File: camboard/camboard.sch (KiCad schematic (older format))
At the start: 7 parts

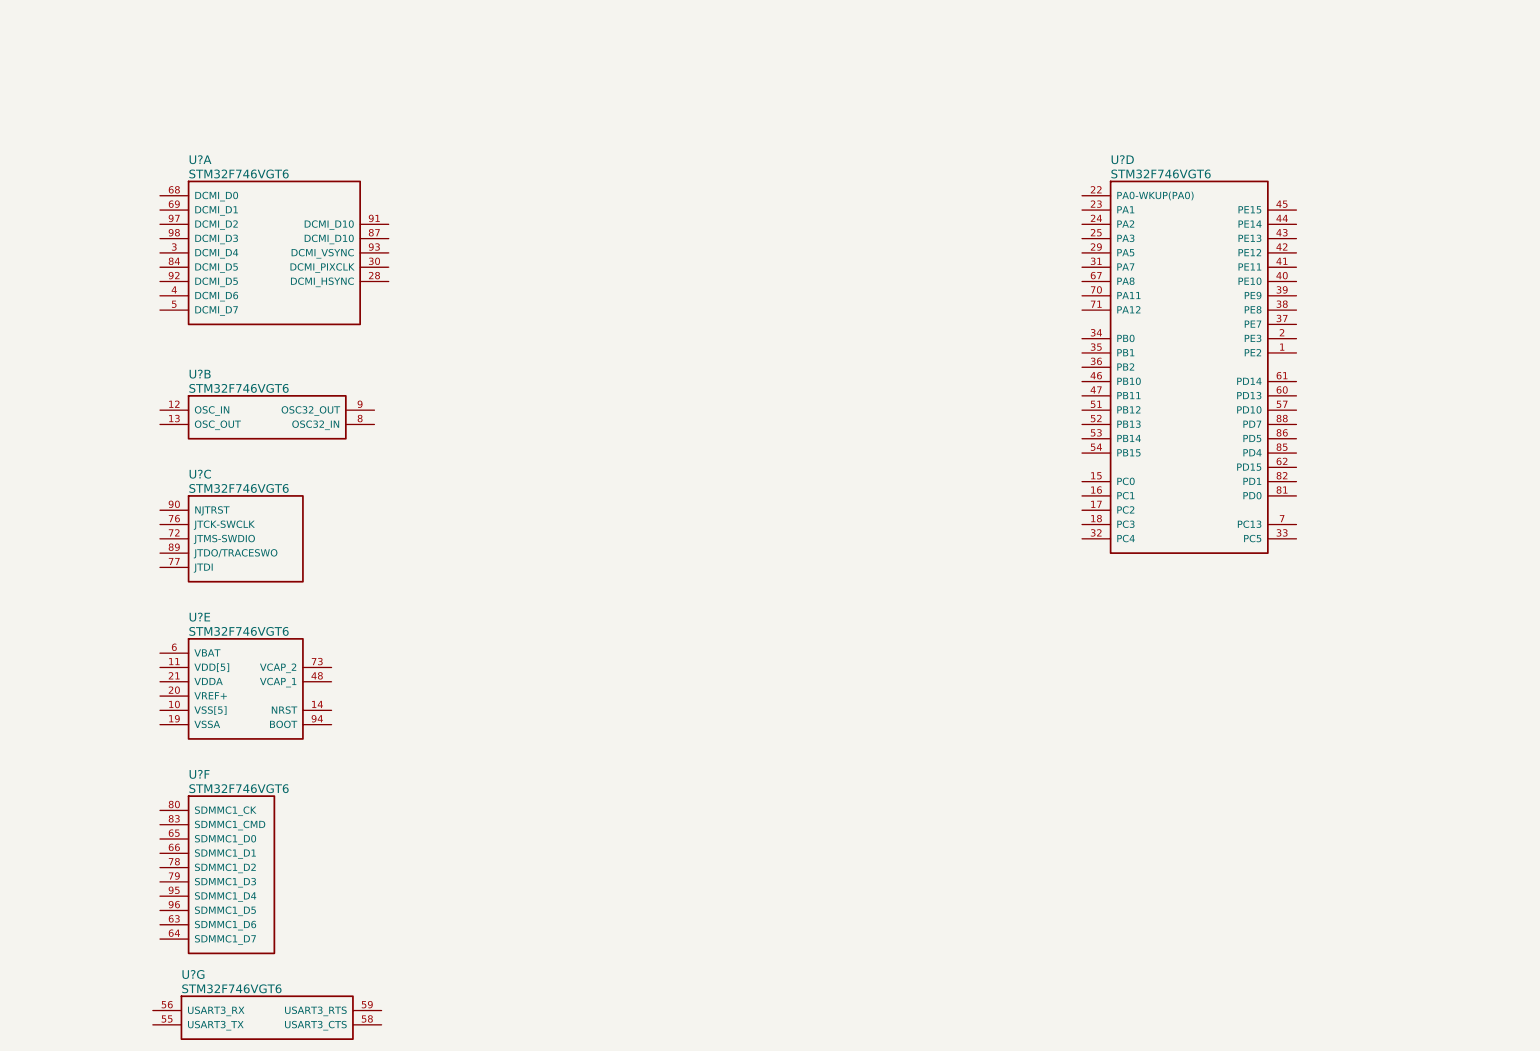
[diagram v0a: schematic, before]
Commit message: added oscillators
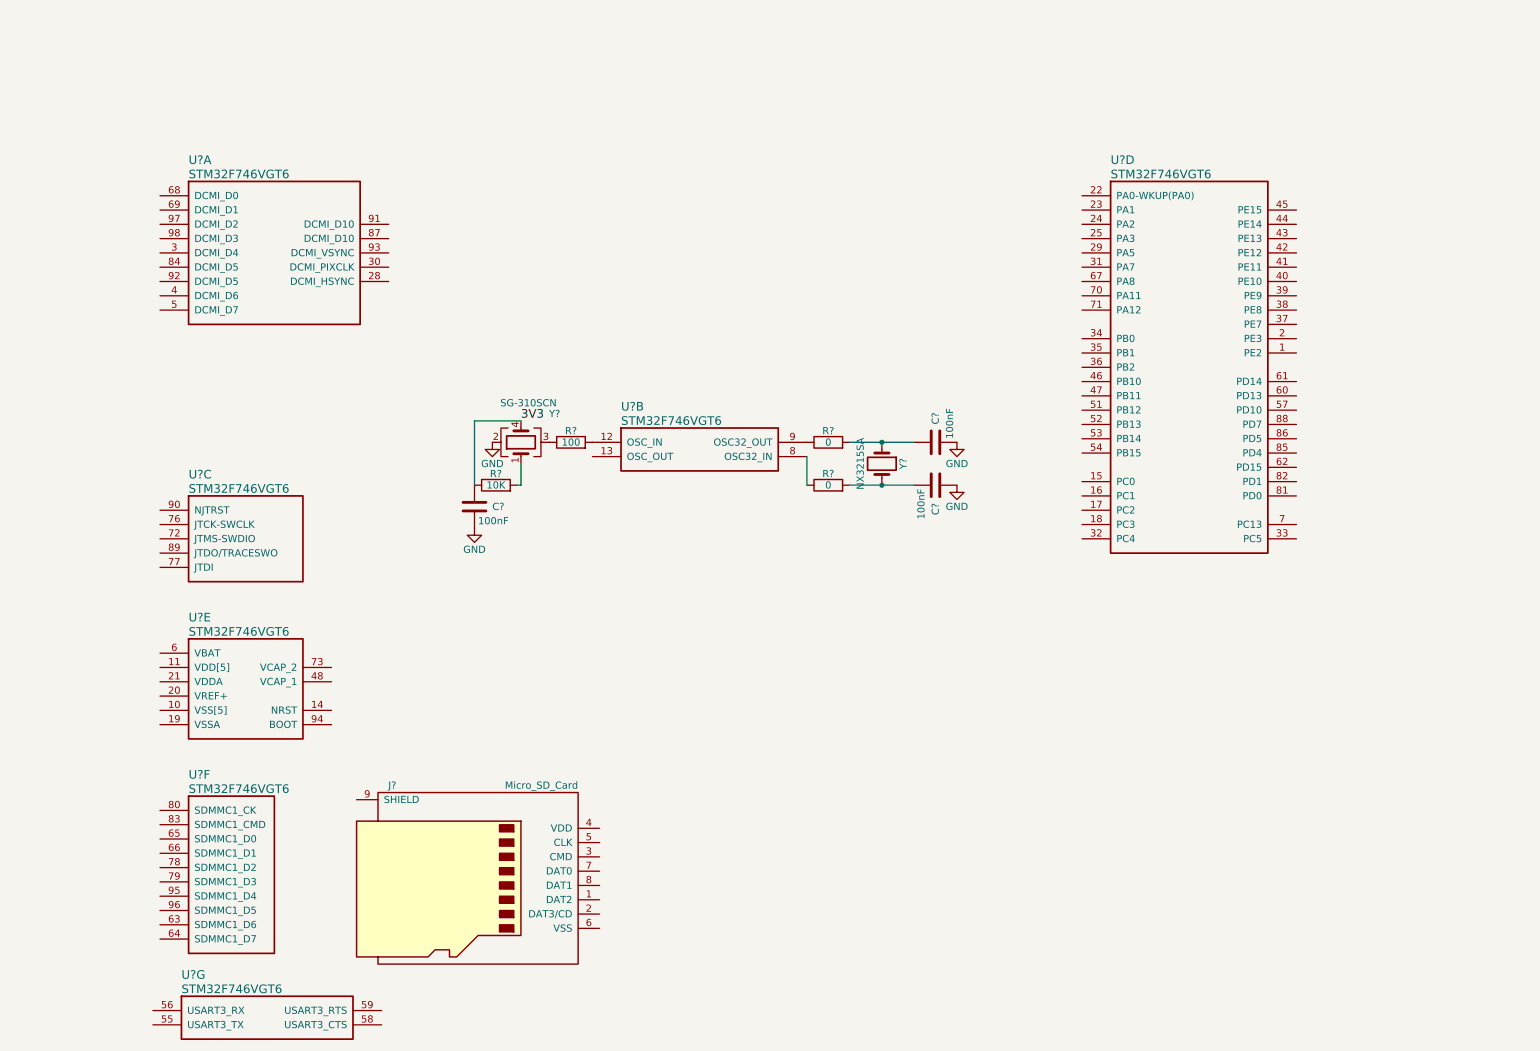
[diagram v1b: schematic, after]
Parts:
- added C? (x3): 100nF, symbol C
- added J?: Micro_SD_Card, symbol Micro_SD_Card
- added R?: 10K, symbol R
- added R?: 100, symbol R
- added R? (x2): 0, symbol R
- added Y?: SG-310SCN, symbol Crystal_GND23
- added Y?: NX3215SA, symbol Crystal
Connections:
- net at U?.12 (OSC_IN): now also R?.2
- net at U?.8 (OSC32_IN): now also R?.1
- net at U?.9 (OSC32_OUT): now also R?.1
- new net: R?.2, Y?.1
- new net: R?.1, Y?.3
- new net: C?.1, R?.2, Y?.1
- new net: C?.2, R?.2, Y?.2
- new net 3V3: C?.1, R?.1, Y?.4
- new net GND: C?.1, C?.2, C?.2, Y?.2
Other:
- moved on the sheet: U?B
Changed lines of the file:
@@
 LIBS:STM32F7x
 LIBS:stm32-v2
+LIBS:114-00841-68-1-nd
 LIBS:camboard-cache
 EELAYER 25 0
@@
 L STM32F746VGT6 U?
 U 2 1 59CAFB26
-P 1300 3250
-F 0 "U?" H 1500 3500 60  0000 L CNN
-F 1 "STM32F746VGT6" H 1500 3400 60  0000 L CNN
-F 2 "" H 1300 3250 60  0001 C CNN
-F 3 "" H 1300 3250 60  0001 C CNN
-	2    1300 3250
+P 4325 3475
+F 0 "U?" H 4525 3725 60  0000 L CNN
+F 1 "STM32F746VGT6" H 4525 3625 60  0000 L CNN
+F 2 "" H 4325 3475 60  0001 C CNN
+F 3 "" H 4325 3475 60  0001 C CNN
+	2    4325 3475
 	1    0    0    -1
 $EndComp
@@
 	1    0    0    -1
 $EndComp
+$Comp
+L Micro_SD_Card J?
+U 1 1 59CBBC6A
+P 3575 6475
+F 0 "J?" H 2925 7075 50  0000 C CNN
+F 1 "Micro_SD_Card" H 4225 7075 50  0000 R CNN
+F 2 "" H 4725 6775 50  0001 C CNN
+F 3 "" H 3575 6475 50  0001 C CNN
+	1    3575 6475
+	1    0    0    -1
+$EndComp
+$Comp
+L Crystal_GND23 Y?
+U 1 1 59CBC17B
+P 3825 3475
+F 0 "Y?" V 4025 3200 50  0000 L CNN
+F 1 "SG-310SCN" V 4100 3225 50  0000 L CNN
+F 2 "" H 3825 3475 50  0001 C CNN
+F 3 "" H 3825 3475 50  0001 C CNN
+	1    3825 3475
+	0    -1   -1   0
+$EndComp
+$Comp
+L Crystal Y?
+U 1 1 59CBC1BE
+P 6350 3625
+F 0 "Y?" H 6350 3775 50  0000 C CNN
+F 1 "NX3215SA" H 6350 3475 50  0000 C CNN
+F 2 "" H 6350 3625 50  0001 C CNN
+F 3 "" H 6350 3625 50  0001 C CNN
+	1    6350 3625
+	0    1    1    0
+$EndComp
+$Comp
+L GND #PWR?
+U 1 1 59CBC3C5
+P 3500 4075
+F 0 "#PWR?" H 3500 3825 50  0001 C CNN
+F 1 "GND" H 3500 3925 50  0000 C CNN
+F 2 "" H 3500 4075 50  0001 C CNN
+F 3 "" H 3500 4075 50  0001 C CNN
+	1    3500 4075
+	1    0    0    -1
+$EndComp
+$Comp
+L R R?
+U 1 1 59CBC4FC
+P 3650 3775
+F 0 "R?" V 3730 3775 50  0000 C CNN
+F 1 "10K" V 3650 3775 50  0000 C CNN
+F 2 "" V 3580 3775 50  0001 C CNN
+F 3 "" H 3650 3775 50  0001 C CNN
+	1    3650 3775
+	0    -1   -1   0
+$EndComp
+$Comp
+L C C?
+U 1 1 59CBC717
+P 3500 3925
+F 0 "C?" H 3625 3925 50  0000 L CNN
+F 1 "100nF" H 3525 3825 50  0000 L CNN
+F 2 "" H 3538 3775 50  0001 C CNN
+F 3 "" H 3500 3925 50  0001 C CNN
+	1    3500 3925
+	1    0    0    -1
+$EndComp
+Text Label 3825 3325 0    60   ~ 0
+3V3
+$Comp
+L GND #PWR?
+U 1 1 59CBC971
+P 3625 3475
+F 0 "#PWR?" H 3625 3225 50  0001 C CNN
+F 1 "GND" H 3625 3325 50  0000 C CNN
+F 2 "" H 3625 3475 50  0001 C CNN
+F 3 "" H 3625 3475 50  0001 C CNN
+	1    3625 3475
+	1    0    0    -1
+$EndComp
+$Comp
+L R R?
+U 1 1 59CBCF2D
+P 4175 3475
+F 0 "R?" V 4255 3475 50  0000 C CNN
+F 1 "100" V 4175 3475 50  0000 C CNN
+F 2 "" V 4105 3475 50  0001 C CNN
+F 3 "" H 4175 3475 50  0001 C CNN
+	1    4175 3475
+	0    -1   -1   0
+$EndComp
+$Comp
+L R R?
+U 1 1 59CBD411
+P 5975 3475
+F 0 "R?" V 6055 3475 50  0000 C CNN
+F 1 "0" V 5975 3475 50  0000 C CNN
+F 2 "" V 5905 3475 50  0001 C CNN
+F 3 "" H 5975 3475 50  0001 C CNN
+	1    5975 3475
+	0    -1   -1   0
+$EndComp
+$Comp
+L R R?
+U 1 1 59CBD485
+P 5975 3775
+F 0 "R?" V 6055 3775 50  0000 C CNN
+F 1 "0" V 5975 3775 50  0000 C CNN
+F 2 "" V 5905 3775 50  0001 C CNN
+F 3 "" H 5975 3775 50  0001 C CNN
+	1    5975 3775
+	0    -1   -1   0
+$EndComp
+Wire Wire Line
+	3825 3325 3500 3325
+Wire Wire Line
+	3500 3325 3500 3775
+Wire Wire Line
+	3800 3775 3825 3775
+Wire Wire Line
+	3825 3775 3825 3625
+Wire Wire Line
+	6125 3475 6575 3475
+Wire Wire Line
+	6125 3775 6575 3775
+$Comp
+L C C?
+U 1 1 59CBD71A
+P 6725 3475
+F 0 "C?" H 6850 3475 50  0000 L CNN
+F 1 "100nF" H 6750 3375 50  0000 L CNN
+F 2 "" H 6763 3325 50  0001 C CNN
+F 3 "" H 6725 3475 50  0001 C CNN
+	1    6725 3475
+	0    -1   -1   0
+$EndComp
+$Comp
+L C C?
+U 1 1 59CBD7BA
+P 6725 3775
+F 0 "C?" H 6850 3775 50  0000 L CNN
+F 1 "100nF" H 6750 3675 50  0000 L CNN
+F 2 "" H 6763 3625 50  0001 C CNN
+F 3 "" H 6725 3775 50  0001 C CNN
+	1    6725 3775
+	0    1    1    0
+$EndComp
+Connection ~ 6350 3475
+Connection ~ 6350 3775
+$Comp
+L GND #PWR?
+U 1 1 59CBD8AB
+P 6875 3475
+F 0 "#PWR?" H 6875 3225 50  0001 C CNN
+F 1 "GND" H 6875 3325 50  0000 C CNN
+F 2 "" H 6875 3475 50  0001 C CNN
+F 3 "" H 6875 3475 50  0001 C CNN
+	1    6875 3475
+	1    0    0    -1
+$EndComp
+$Comp
+L GND #PWR?
+U 1 1 59CBD8FA
+P 6875 3775
+F 0 "#PWR?" H 6875 3525 50  0001 C CNN
+F 1 "GND" H 6875 3625 50  0000 C CNN
+F 2 "" H 6875 3775 50  0001 C CNN
+F 3 "" H 6875 3775 50  0001 C CNN
+	1    6875 3775
+	1    0    0    -1
+$EndComp
+Wire Wire Line
+	5825 3575 5825 3775
 $EndSCHEMATC

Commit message: fixed wrong library reference and added power select
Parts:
- removed J?: Micro_SD_Card, symbol Micro_SD_Card
- added BT?: Battery, symbol Battery
- added SW?: JS202011SCQN, symbol SW_DPDT_x2
- added U?: MCP1703A-3302_SOT23, TO_SOT_Packages_SMD:SOT-23, symbol MCP1703A-3302_SOT23
- added U?: FT230XS, SSOP-16, symbol FT230XS
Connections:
- net labels added: USB_3V3
- wire segments 7 -> 9
- no-connect marks 0 -> 5
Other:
- moved on the sheet: C?, R?, U?A, U?B, U?C, U?E, U?F, U?G, Y?

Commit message: more connections
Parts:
- removed BT?: Battery, symbol Battery
- removed SW?: JS202011SCQN, symbol SW_DPDT_x2
- added J?: Micro_SD_Card, symbol Micro_SD_Card
- added SW?: SW_DPDT_x2, Buttons_Switches_THT:SW_CuK_JS202011CQN_DPDT_Straight, symbol SW_DPDT_x2
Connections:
- net labels added: +3V3, USB_5V, VIN
- net labels removed: 3V3, USB_3V3
- wire segments 9 -> 19
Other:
- moved on the sheet: U?, U?F, U?G
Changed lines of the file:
@@
 L STM32F746VGT6 U?
 U 7 1 59CAFE6F
-P 625 6800
-F 0 "U?" H 825 7050 60  0000 L CNN
-F 1 "STM32F746VGT6" H 825 6950 60  0000 L CNN
-F 2 "" H 625 6800 60  0001 C CNN
-F 3 "" H 625 6800 60  0001 C CNN
-	7    625  6800
-	1    0    0    -1
+P 7125 4425
+F 0 "U?" H 7350 4150 60  0000 L CNN
+F 1 "STM32F746VGT6" H 7550 4150 60  0000 L CNN
+F 2 "" H 7125 4425 60  0001 C CNN
+F 3 "" H 7125 4425 60  0001 C CNN
+	7    7125 4425
+	-1   0    0    -1
 $EndComp
 $Comp
@@
 P 7700 5400
 F 0 "Y?" V 7900 5125 50  0000 L CNN
-F 1 "SG-310SCN" V 7975 5150 50  0000 L CNN
+F 1 "SG-310SCN" V 8150 5200 50  0000 L CNN
 F 2 "" H 7700 5400 50  0001 C CNN
 F 3 "" H 7700 5400 50  0001 C CNN
@@
 	1    0    0    -1
 $EndComp
-Text Label 7700 5250 0    60   ~ 0
-3V3
 $Comp
 L GND #PWR?
@@
 Wire Wire Line
 	9700 5500 9700 5700
-NoConn ~ 775  6300
-NoConn ~ 775  6200
+NoConn ~ 3900 6925
+NoConn ~ 3900 6825
 $Comp
 L STM32F746VGT6 U?
 U 6 1 59CAFD02
-P 775 5400
-F 0 "U?" H 975 5650 60  0000 L CNN
-F 1 "STM32F746VGT6" H 975 5550 60  0000 L CNN
-F 2 "" H 775 5400 60  0001 C CNN
-F 3 "" H 775 5400 60  0001 C CNN
-	6    775  5400
-	1    0    0    -1
-$EndComp
-NoConn ~ 775  6100
-NoConn ~ 775  6000
+P 3900 6025
+F 0 "U?" H 4100 6275 60  0000 L CNN
+F 1 "STM32F746VGT6" H 4100 6175 60  0000 L CNN
+F 2 "" H 3900 6025 60  0001 C CNN
+F 3 "" H 3900 6025 60  0001 C CNN
+	6    3900 6025
+	1    0    0    -1
+$EndComp
+NoConn ~ 3900 6725
+NoConn ~ 3900 6625
 $Comp
 L MCP1703A-3302_SOT23 U?
 U 1 1 59CBD041
-P 1150 850
-F 0 "U?" H 1000 975 50  0000 C CNN
-F 1 "MCP1703A-3302_SOT23" H 575 1075 50  0000 L CNN
-F 2 "TO_SOT_Packages_SMD:SOT-23" H 1150 1050 50  0001 C CNN
-F 3 "" H 1150 800 50  0001 C CNN
-	1    1150 850
+P 2725 875
+F 0 "U?" H 2575 1000 50  0000 C CNN
+F 1 "MCP1703A-3302_SOT23" H 2300 1175 50  0000 L CNN
+F 2 "TO_SOT_Packages_SMD:SOT-23" H 2725 1075 50  0001 C CNN
+F 3 "" H 2725 825 50  0001 C CNN
+	1    2725 875
 	1    0    0    -1
 $EndComp
@@
 	1    0    0    -1
 $EndComp
-$Comp
-L Battery BT?
-U 1 1 59CBD1E1
-P 850 1050
-F 0 "BT?" H 600 1150 50  0000 L CNN
-F 1 "Battery" H 500 1050 50  0000 L CNN
-F 2 "" V 850 1110 50  0001 C CNN
-F 3 "" V 850 1110 50  0001 C CNN
-	1    850  1050
-	1    0    0    -1
-$EndComp
-Wire Wire Line
-	850  1250 1150 1250
-Wire Wire Line
-	1150 1250 1150 1150
+Text Label 2025 975  2    60   ~ 0
+USB_5V
+$Comp
+L GND #PWR?
+U 1 1 59CBCD24
+P 4725 5325
+F 0 "#PWR?" H 4725 5075 50  0001 C CNN
+F 1 "GND" H 4725 5175 50  0000 C CNN
+F 2 "" H 4725 5325 50  0001 C CNN
+F 3 "" H 4725 5325 50  0001 C CNN
+	1    4725 5325
+	1    0    0    -1
+$EndComp
+$Comp
+L GND #PWR?
+U 1 1 59CBCD6B
+P 4925 5325
+F 0 "#PWR?" H 4925 5075 50  0001 C CNN
+F 1 "GND" H 4925 5175 50  0000 C CNN
+F 2 "" H 4925 5325 50  0001 C CNN
+F 3 "" H 4925 5325 50  0001 C CNN
+	1    4925 5325
+	1    0    0    -1
+$EndComp
+Wire Wire Line
+	5525 4225 7200 4225
+Wire Wire Line
+	7200 4225 7200 4525
+Wire Wire Line
+	7200 4525 7125 4525
+Wire Wire Line
+	7125 4425 7125 4300
+Wire Wire Line
+	7125 4300 5525 4300
+Wire Wire Line
+	5525 4300 5525 4325
 $Comp
 L SW_DPDT_x2 SW?
-U 1 1 59CBE085
-P 1650 950
-F 0 "SW?" H 1525 1150 50  0000 C CNN
-F 1 "JS202011SCQN" H 1475 1275 50  0000 C CNN
-F 2 "" H 1650 950 50  0001 C CNN
-F 3 "" H 1650 950 50  0001 C CNN
-	1    1650 950
+U 1 1 59CBC80C
+P 2225 875
+F 0 "SW?" H 2225 1045 50  0000 C CNN
+F 1 "SW_DPDT_x2" H 2225 675 50  0000 C CNN
+F 2 "Buttons_Switches_THT:SW_CuK_JS202011CQN_DPDT_Straight" H 2325 1125 50  0001 C CNN
+F 3 "" H 2225 1045 50  0001 C CNN
+	1    2225 875
 	-1   0    0    1
 $EndComp
-Text Label 1850 950  0    60   ~ 0
-3V3
-Text Label 4125 4225 2    60   ~ 0
-USB_3V3
-Text Label 1450 1050 3    60   ~ 0
-USB_3V3
+Text Label 2025 775  2    60   ~ 0
+VIN
+$Comp
+L GND #PWR?
+U 1 1 59CBD66A
+P 2725 1175
+F 0 "#PWR?" H 2725 925 50  0001 C CNN
+F 1 "GND" H 2725 1025 50  0000 C CNN
+F 2 "" H 2725 1175 50  0001 C CNN
+F 3 "" H 2725 1175 50  0001 C CNN
+	1    2725 1175
+	1    0    0    -1
+$EndComp
+$Comp
+L +3V3 #PWR?
+U 1 1 59CBD92A
+P 3025 875
+F 0 "#PWR?" H 3025 725 50  0001 C CNN
+F 1 "+3V3" H 3025 1015 50  0000 C CNN
+F 2 "" H 3025 875 50  0001 C CNN
+F 3 "" H 3025 875 50  0001 C CNN
+	1    3025 875
+	0    1    1    0
+$EndComp
+$Comp
+L +3V3 #PWR?
+U 1 1 59CBDBE9
+P 7700 5250
+F 0 "#PWR?" H 7700 5100 50  0001 C CNN
+F 1 "+3V3" H 7700 5390 50  0000 C CNN
+F 2 "" H 7700 5250 50  0001 C CNN
+F 3 "" H 7700 5250 50  0001 C CNN
+	1    7700 5250
+	1    0    0    -1
+$EndComp
+$Comp
+L Micro_SD_Card J?
+U 1 1 59CBE1D5
+P 2875 6225
+F 0 "J?" H 2225 6825 50  0000 C CNN
+F 1 "Micro_SD_Card" H 3525 6825 50  0000 R CNN
+F 2 "" V 2575 7175 50  0001 C CNN
+F 3 "" H 2775 6125 50  0001 C CNN
+	1    2875 6225
+	1    0    0    -1
+$EndComp
+Wire Wire Line
+	3675 6025 3900 6025
+Wire Wire Line
+	3900 6125 3675 6125
+Wire Wire Line
+	3675 6225 3900 6225
+Wire Wire Line
+	3675 6325 3900 6325
+Wire Wire Line
+	3900 6425 3675 6425
+Wire Wire Line
+	3675 6525 3900 6525
 $EndSCHEMATC
